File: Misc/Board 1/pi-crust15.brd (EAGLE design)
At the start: 101.6 x 78.8 mm, 40 parts, among them IC10 40193N, IC2 74LS595D, IC3 74LS595D, IC4 74LS595D, IC5 74LS595D, IC6 74LS595D, IC7 74LS595D, IC8 74AC11008, U1 AD9983AKSTZ_140, U2 SN54LS253_J_16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

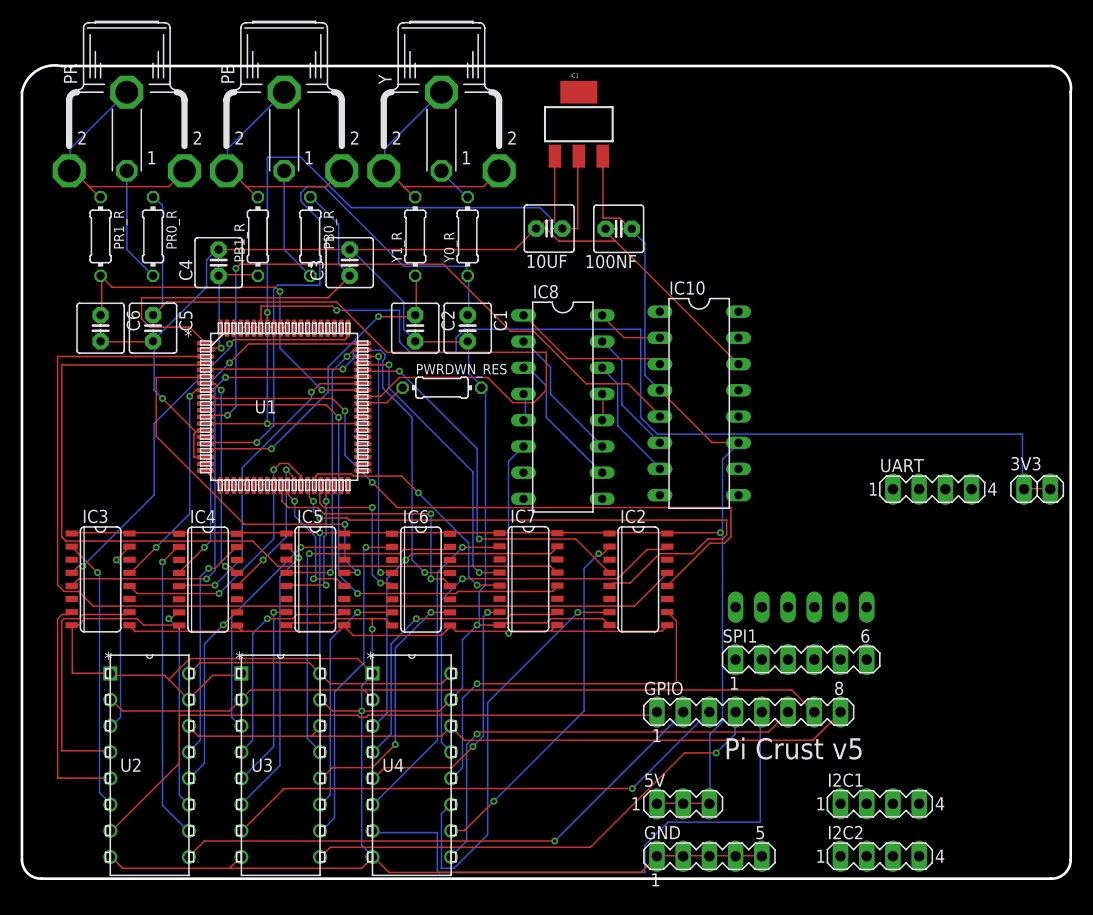
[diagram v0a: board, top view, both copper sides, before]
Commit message: Board Update 7
Rather than using the TOBU3, I have used a 1x1 pin header and used the
dimensions of RCJ-32265 (our RCA jack).  I also had to move some
resistors and capacitors around because of the order of input.  All else
remains the same as in 14
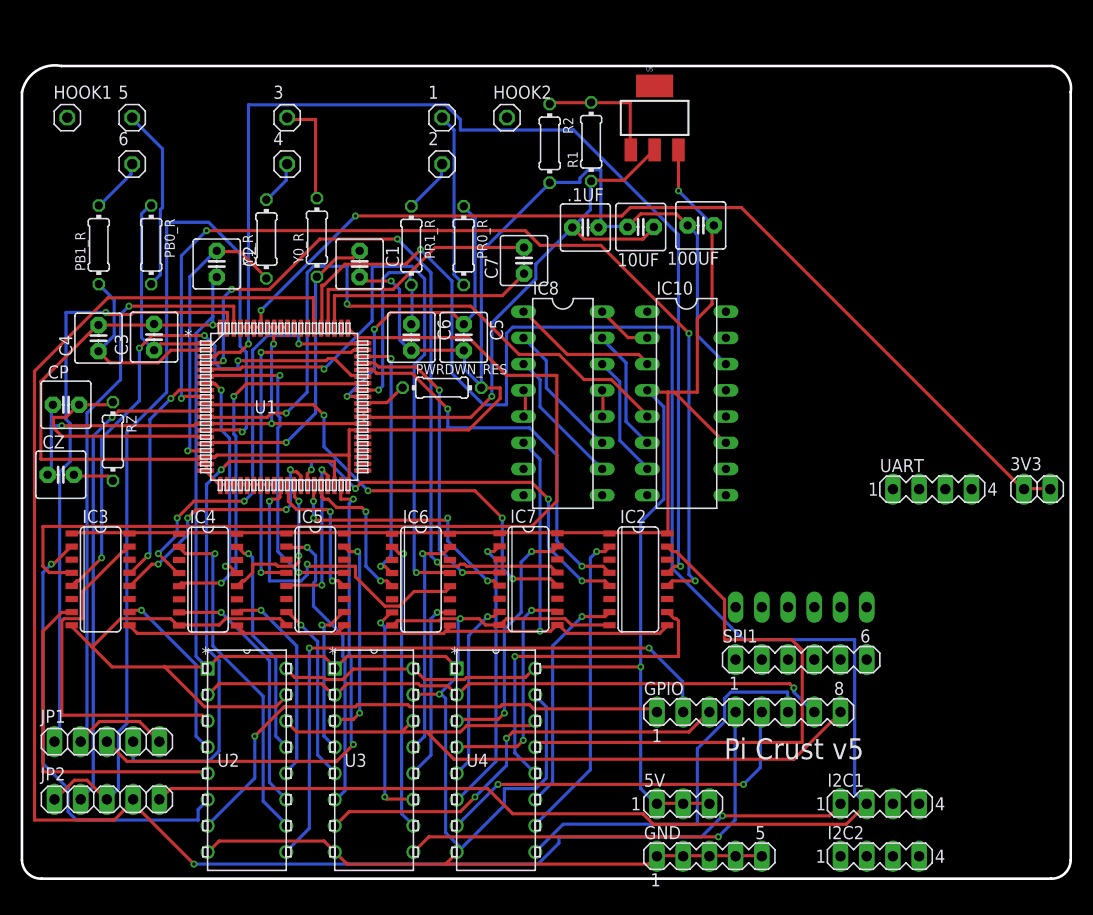
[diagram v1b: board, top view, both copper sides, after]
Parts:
- removed 100NF: (no value), capacitor-wima:C2.5-5
- removed IC1: (no value), SparkFun-PowerIC:SOT223
- removed PB, PR, Y: TOBU3, con-hirschmann:TOBU3
- added .1UF, 100UF: (no value), capacitor-wima:C2.5-5
- added 1, 2, 3, 4, 5, 6, HOOK1, HOOK2: (no value), pinhead:1X01
- added C7: 10u, capacitor-wima:C2.5-5
- added CP: 8.2nF, capacitor-wima:C2.5-5
- added CZ: 82nF, capacitor-wima:C2.5-5
- added JP1, JP2: (no value), pinhead:1X05
- added R1: 240, rcl:0204/7
- added R2: 105, rcl:0204/7
- added RZ: 1.5k, eagle-ltspice:0204/7
- added U5: V_REG_317SMD, SparkFun-PowerIC:SOT223
- moved C5 30.1 mm to (42.8, 52.5)
- moved C6 30.1 mm to (37.7, 52.5)
- moved PR0_R 30.1 mm to (42.8, 61.3)
- moved PR1_R 30.1 mm to (37.7, 61.3)
- moved C3 20.3 mm to (12.8, 52.5)
- moved C2 20.2 mm to (18.9, 59.6)
- moved PB0_R 15.4 mm to (12.5, 61.4)
- moved PB1_R 15.4 mm to (7.44, 61.4)
- moved Y0_R 14.6 mm to (28.6, 62.1)
- moved Y1_R 14.4 mm to (23.7, 62.0)
- moved C4 13.7 mm to (7.42, 52.4)
- moved C1 12.2 mm to (32.7, 59.6)
- moved U2 9.44 mm to (25.6, 2.59)
- moved U3 9.06 mm to (37.9, 2.59)
- moved 10UF 8.87 mm to (59.9, 63.1)
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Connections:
- new net CLAMP: JP2.2, U1.73
- new net EXTCLK/COAST: JP2.1, JP2.3, U1.72
- new net FILT: CP.2, RZ.1, U1.78
- new net HSOUT: JP1.4, U1.23
- new net HSYNC0: JP1.3, U1.70
- new net N$1: CZ.2, RZ.2
- new net REFHI: C7.1, U1.20
- new net REFLO: C7.2, U1.18
- new net SCL: I2C1.2, JP2.5, U1.67
- new net SDA: I2C1.1, JP2.4, U1.66
- new net U1: R1.2, R2.1, U5.1
- new net VSOUT/A0: JP1.2, JP1.5, U1.22
- new net VSYNC0: JP1.1, U1.71
- net 1.8V: now also .1UF.1, CP.1, CZ.1, R1.1, U5.2; no longer IC1.2
- net 5V: now also 100UF.1, U5.3; no longer 100NF.1, IC1.3
- net GND_WIRE: now also .1UF.2, 100UF.2, R2.2, U1.21, U1.68, U1.69; no longer 100NF.2, IC1.1, U1.72
- net PBIN_0: now also 5.1; no longer PB.1
- net PBIN_1: now also 6.1; no longer PB.2, PB.2@1, PB.2@2
- net PRIN_0: now also 1.1; no longer PR.1
- net PRIN_1: now also 2.1; no longer PR.2, PR.2@1, PR.2@2
- net YIN_0: now also 3.1; no longer Y.1
- net YIN_1: now also 4.1; no longer Y.2, Y.2@1, Y.2@2
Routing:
- net SCL: track 0.00 -> 189.7 mm, vias 0 -> 1
- net SDA: track 0.00 -> 161.1 mm, vias 0 -> 2
- net EXTCLK/COAST: track 0.00 -> 94.7 mm, vias 0 -> 1
- net GND_WIRE: track 345.8 -> 413.5 mm
- net VSOUT/A0: track 0.00 -> 65.7 mm, vias 0 -> 1
- net VSYNC0: track 0.00 -> 59.7 mm, vias 0 -> 1
- net HSOUT: track 0.00 -> 52.6 mm, vias 0 -> 1
- net HSYNC0: track 0.00 -> 52.0 mm, vias 0 -> 2
- net R7: track 41.3 -> 92.0 mm, vias 2 -> 0
- net CLAMP: track 0.00 -> 47.6 mm, vias 0 -> 1
- net RIN0_ADC: track 76.6 -> 31.3 mm, vias 0 -> 2
- net B6: track 68.8 -> 97.7 mm, vias 2 -> 4
- net GIN0_ADC: track 59.3 -> 30.5 mm
- net REFLO: track 0.00 -> 24.4 mm
- net FILT: track 0.00 -> 22.5 mm
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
